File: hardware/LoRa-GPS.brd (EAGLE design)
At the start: 50.8 x 17.8 mm, 30 parts, among them J1 10118193-0001LF, Q1 IRLML6402, U1 MCP1703-3302E/CB, Y1 CRYSTAL.ABS07

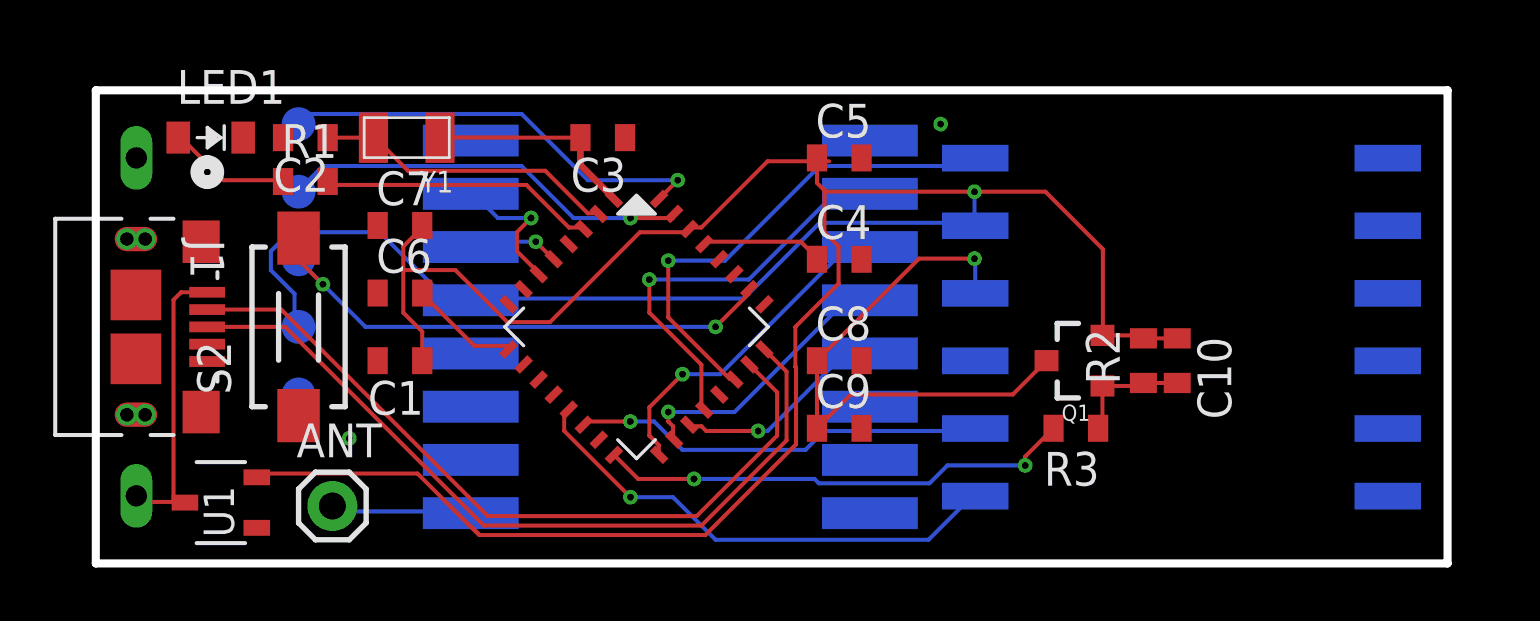
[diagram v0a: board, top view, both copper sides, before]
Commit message: DRC correct. CAM output
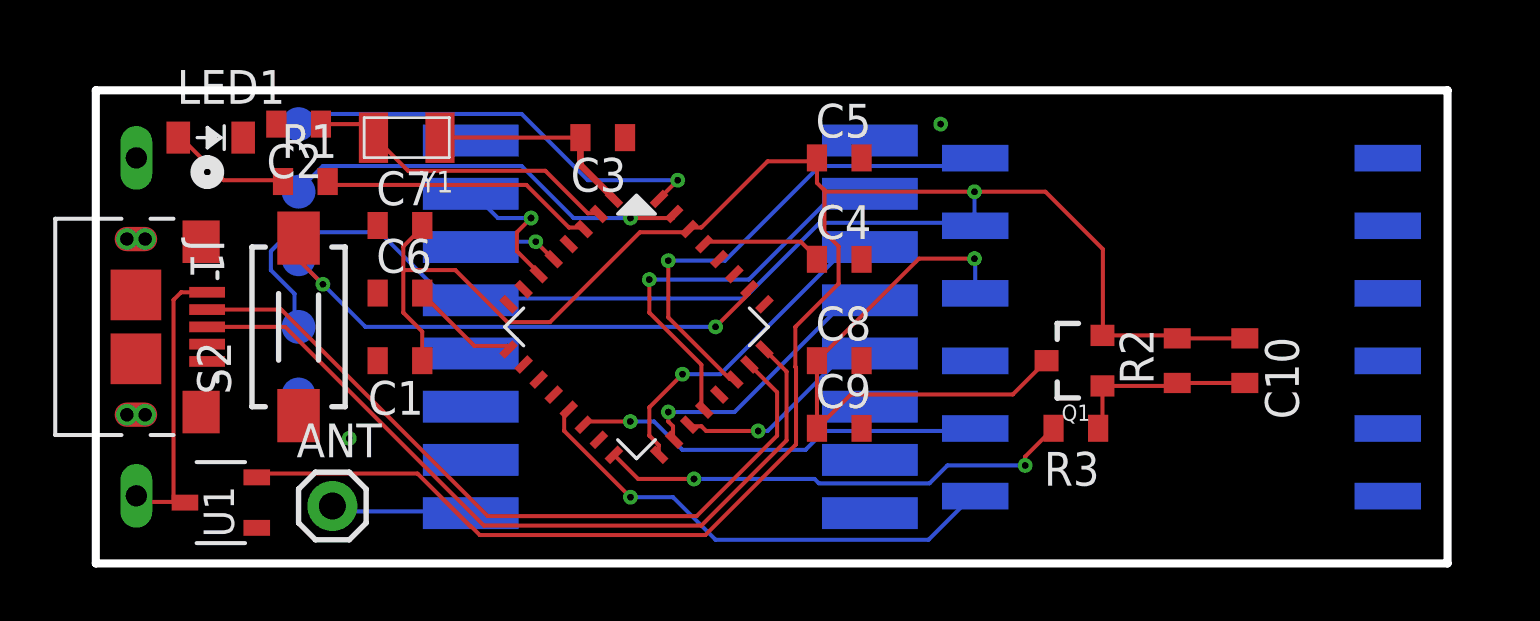
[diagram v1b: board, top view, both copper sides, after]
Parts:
- moved C10 2.54 mm to (43.2, 7.62)
- moved R2 1.27 mm to (40.6, 7.62)
- moved C2 0.57 mm to (7.62, 16.5)
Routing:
- net N$8: track 4.51 -> 7.05 mm
- net VCC: track 111.3 -> 112.8 mm
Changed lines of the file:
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@@
 <drawing>
 <settings>
-<setting alwaysvectorfont="yes"/>
+<setting alwaysvectorfont="no"/>
 <setting keepoldvectorfont="yes"/>
 <setting verticaltext="up"/>
@@
 <layer number="37" name="tTest" color="7" fill="1" visible="no" active="yes"/>
 <layer number="38" name="bTest" color="7" fill="1" visible="no" active="yes"/>
-<layer number="39" name="tKeepout" color="4" fill="11" visible="no" active="yes"/>
+<layer number="39" name="tKeepout" color="4" fill="11" visible="yes" active="yes"/>
 <layer number="40" name="bKeepout" color="1" fill="11" visible="no" active="yes"/>
 <layer number="41" name="tRestrict" color="4" fill="10" visible="no" active="yes"/>
@@
 <attribute name="VALUE" x="12.319" y="9.652" size="1.27" layer="27" rot="R180"/>
 </element>
-<element name="C2" library="nootropicdesign" package="C0603-THINCREAM" value="18pF" x="7.874" y="16.002" smashed="yes" rot="R180">
-<attribute name="MF" value="" x="7.874" y="16.002" size="1.778" layer="27" rot="R180" display="off"/>
-<attribute name="MPN" value="" x="7.874" y="16.002" size="1.778" layer="27" rot="R180" display="off"/>
-<attribute name="NAME" x="8.763" y="15.24" size="1.27" layer="25" rot="R180"/>
-<attribute name="OC_FARNELL" value="unknown" x="7.874" y="16.002" size="1.778" layer="27" rot="R180" display="off"/>
-<attribute name="VALUE" x="8.763" y="18.034" size="1.27" layer="27" rot="R180"/>
+<element name="C2" library="nootropicdesign" package="C0603-THINCREAM" value="18pF" x="7.62" y="16.51" smashed="yes" rot="R180">
+<attribute name="MF" value="" x="7.62" y="16.51" size="1.778" layer="27" rot="R180" display="off"/>
+<attribute name="MPN" value="" x="7.62" y="16.51" size="1.778" layer="27" rot="R180" display="off"/>
+<attribute name="NAME" x="8.509" y="15.748" size="1.27" layer="25" rot="R180"/>
+<attribute name="OC_FARNELL" value="unknown" x="7.62" y="16.51" size="1.778" layer="27" rot="R180" display="off"/>
+<attribute name="VALUE" x="8.509" y="18.542" size="1.27" layer="27" rot="R180"/>
 </element>
 <element name="C3" library="nootropicdesign" package="C0603-THINCREAM" value="18pF" x="19.05" y="16.002" smashed="yes" rot="R180">
@@
 <attribute name="VALUE" x="36.83" y="9.271" size="0.6096" layer="27" font="vector" ratio="20" rot="R180" align="top-center"/>
 </element>
-<element name="C10" library="nootropicdesign" package="C0603-THINCREAM" value="4.7uF" x="40.64" y="7.62" smashed="yes" rot="R270">
-<attribute name="MF" value="" x="40.64" y="7.62" size="1.778" layer="27" rot="R270" display="off"/>
-<attribute name="MPN" value="" x="40.64" y="7.62" size="1.778" layer="27" rot="R270" display="off"/>
-<attribute name="NAME" x="41.402" y="8.509" size="1.27" layer="25" rot="R270"/>
-<attribute name="OC_FARNELL" value="unknown" x="40.64" y="7.62" size="1.778" layer="27" rot="R270" display="off"/>
-<attribute name="VALUE" x="38.608" y="8.509" size="1.27" layer="27" rot="R270"/>
-</element>
-<element name="R2" library="nootropicdesign" package="R0603-THINCREAM" value="470" x="39.37" y="7.62" smashed="yes" rot="R90">
-<attribute name="MF" value="" x="39.37" y="7.62" size="1.778" layer="27" rot="R90" display="off"/>
-<attribute name="MPN" value="" x="39.37" y="7.62" size="1.778" layer="27" rot="R90" display="off"/>
-<attribute name="NAME" x="38.481" y="6.731" size="1.27" layer="25" rot="R90"/>
-<attribute name="OC_FARNELL" value="unknown" x="39.37" y="7.62" size="1.778" layer="27" rot="R90" display="off"/>
-<attribute name="VALUE" x="41.402" y="6.731" size="1.27" layer="27" rot="R90"/>
+<element name="C10" library="nootropicdesign" package="C0603-THINCREAM" value="4.7uF" x="43.18" y="7.62" smashed="yes" rot="R270">
+<attribute name="MF" value="" x="43.18" y="7.62" size="1.778" layer="27" rot="R270" display="off"/>
+<attribute name="MPN" value="" x="43.18" y="7.62" size="1.778" layer="27" rot="R270" display="off"/>
+<attribute name="NAME" x="43.942" y="8.509" size="1.27" layer="25" rot="R270"/>
+<attribute name="OC_FARNELL" value="unknown" x="43.18" y="7.62" size="1.778" layer="27" rot="R270" display="off"/>
+<attribute name="VALUE" x="41.148" y="8.509" size="1.27" layer="27" rot="R270"/>
+</element>
+<element name="R2" library="nootropicdesign" package="R0603-THINCREAM" value="470" x="40.64" y="7.62" smashed="yes" rot="R90">
+<attribute name="MF" value="" x="40.64" y="7.62" size="1.778" layer="27" rot="R90" display="off"/>
+<attribute name="MPN" value="" x="40.64" y="7.62" size="1.778" layer="27" rot="R90" display="off"/>
+<attribute name="NAME" x="39.751" y="6.731" size="1.27" layer="25" rot="R90"/>
+<attribute name="OC_FARNELL" value="unknown" x="40.64" y="7.62" size="1.778" layer="27" rot="R90" display="off"/>
+<attribute name="VALUE" x="42.672" y="6.731" size="1.27" layer="27" rot="R90"/>
 </element>
 <element name="R3" library="nootropicdesign" package="R0603-THINCREAM" value="2K2" x="36.83" y="5.08" smashed="yes" rot="R180">
@@
 <contactref element="TP2" pad="P$1"/>
 <via x="33.02" y="13.97" extent="1-16" drill="0.254"/>
-<wire x1="33.02" y1="13.97" x2="33.05" y2="13.94" width="0.254" layer="16"/>
 <wire x1="12.2682" y1="8.7122" x2="12.2682" y2="7.62" width="0.1524" layer="1"/>
 <wire x1="11.557" y1="9.4234" x2="12.2682" y2="8.7122" width="0.1524" layer="1"/>
@@
 <wire x1="14.0462" y1="9.9568" x2="14.09" y2="9.89" width="0.1524" layer="16"/>
 <wire x1="12.0904" y1="3.3782" x2="6.223" y2="3.3782" width="0.1524" layer="1"/>
-<wire x1="14.4018" y1="1.0668" x2="14.0843" y2="1.3843" width="0.1524" layer="1"/>
 <wire x1="14.0843" y1="1.3843" x2="12.0904" y2="3.3782" width="0.1524" layer="1"/>
 <wire x1="6.223" y1="3.3782" x2="6.049" y2="3.236" width="0.1524" layer="1"/>
@@
 <wire x1="32.893" y1="12.8016" x2="27.2034" y2="12.8016" width="0.1524" layer="16"/>
 <wire x1="14.224" y1="9.9568" x2="14.09" y2="9.89" width="0.1524" layer="16"/>
-<wire x1="27.559" y1="15.113" x2="27.2034" y2="15.113" width="0.1524" layer="1"/>
-<wire x1="27.2034" y1="15.113" x2="27.1018" y2="15.24" width="0.1524" layer="1"/>
 <contactref element="Q1" pad="2"/>
 <contactref element="C10" pad="1"/>
 <contactref element="R2" pad="2"/>
 <contactref element="GPS" pad="5"/>
-<wire x1="37.83" y1="8.57" x2="39.2582" y2="8.57" width="0.1524" layer="1"/>
-<wire x1="39.2582" y1="8.57" x2="39.37" y2="8.4582" width="0.1524" layer="1"/>
-<wire x1="39.37" y1="8.4582" x2="40.64" y2="8.4582" width="0.1524" layer="1"/>
+<wire x1="37.83" y1="8.57" x2="40.5282" y2="8.57" width="0.1524" layer="1"/>
+<wire x1="40.5282" y1="8.57" x2="40.64" y2="8.4582" width="0.1524" layer="1"/>
+<wire x1="40.64" y1="8.4582" x2="43.18" y2="8.4582" width="0.1524" layer="1"/>
 <wire x1="27.1018" y1="15.24" x2="27.1018" y2="14.3002" width="0.1524" layer="1"/>
 <wire x1="27.432" y1="13.97" x2="33.02" y2="13.97" width="0.1524" layer="1"/>
@@
 <wire x1="3.2004" y1="2.3114" x2="3.349" y2="2.286" width="0.1524" layer="1"/>
 <wire x1="1.6002" y1="2.4892" x2="1.524" y2="2.54" width="0.1524" layer="1"/>
-<wire x1="1.6002" y1="2.667" x2="1.524" y2="2.54" width="0.1524" layer="16"/>
 <contactref element="J1" pad="1"/>
 <wire x1="4.1827" y1="10.19" x2="3.205" y2="10.19" width="0.1524" layer="1"/>
@@
 <wire x1="18.8468" y1="13.1572" x2="18.905784375" y2="13.132640625" width="0.1524" layer="1"/>
 <wire x1="10.4902" y1="16.002" x2="10.434" y2="16.002" width="0.1524" layer="1"/>
-<wire x1="10.434" y1="16.002" x2="8.7122" y2="16.002" width="0.1524" layer="1"/>
+<wire x1="10.434" y1="16.002" x2="9.926" y2="16.51" width="0.1524" layer="1"/>
+<wire x1="9.926" y1="16.51" x2="8.4582" y2="16.51" width="0.1524" layer="1"/>
 </signal>
 <signal name="N$3">
@@
 <contactref element="C3" pad="2"/>
 <contactref element="SAMD21" pad="1"/>
-<wire x1="19.3802" y1="13.8684" x2="19.45505625" y2="13.728909375" width="0.1524" layer="1"/>
 <wire x1="19.45505625" y1="13.728909375" x2="19.47146875" y2="13.698325" width="0.1524" layer="1"/>
 <wire x1="12.934" y1="16.002" x2="18.2118" y2="16.002" width="0.1524" layer="1"/>
@@
 <contactref element="Q1" pad="1"/>
 <contactref element="R3" pad="1"/>
-<wire x1="40.64" y1="6.7818" x2="39.37" y2="6.7818" width="0.1524" layer="1"/>
-<wire x1="39.37" y1="6.7818" x2="39.2582" y2="6.67" width="0.1524" layer="1"/>
-<wire x1="39.2582" y1="6.67" x2="37.83" y2="6.67" width="0.1524" layer="1"/>
+<wire x1="43.18" y1="6.7818" x2="40.64" y2="6.7818" width="0.1524" layer="1"/>
+<wire x1="40.64" y1="6.7818" x2="40.5282" y2="6.67" width="0.1524" layer="1"/>
+<wire x1="40.5282" y1="6.67" x2="37.83" y2="6.67" width="0.1524" layer="1"/>
 <wire x1="37.83" y1="6.67" x2="37.83" y2="5.2418" width="0.1524" layer="1"/>
 <wire x1="37.83" y1="5.2418" x2="37.6682" y2="5.08" width="0.1524" layer="1"/>
@@
 <mfgpreviewcolor name="substratecolor" color="0xFF786E46"/>
 </mfgpreviewcolors>
+<errors>
+</errors>
 </board>
 </drawing>

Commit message: 470 to 47k
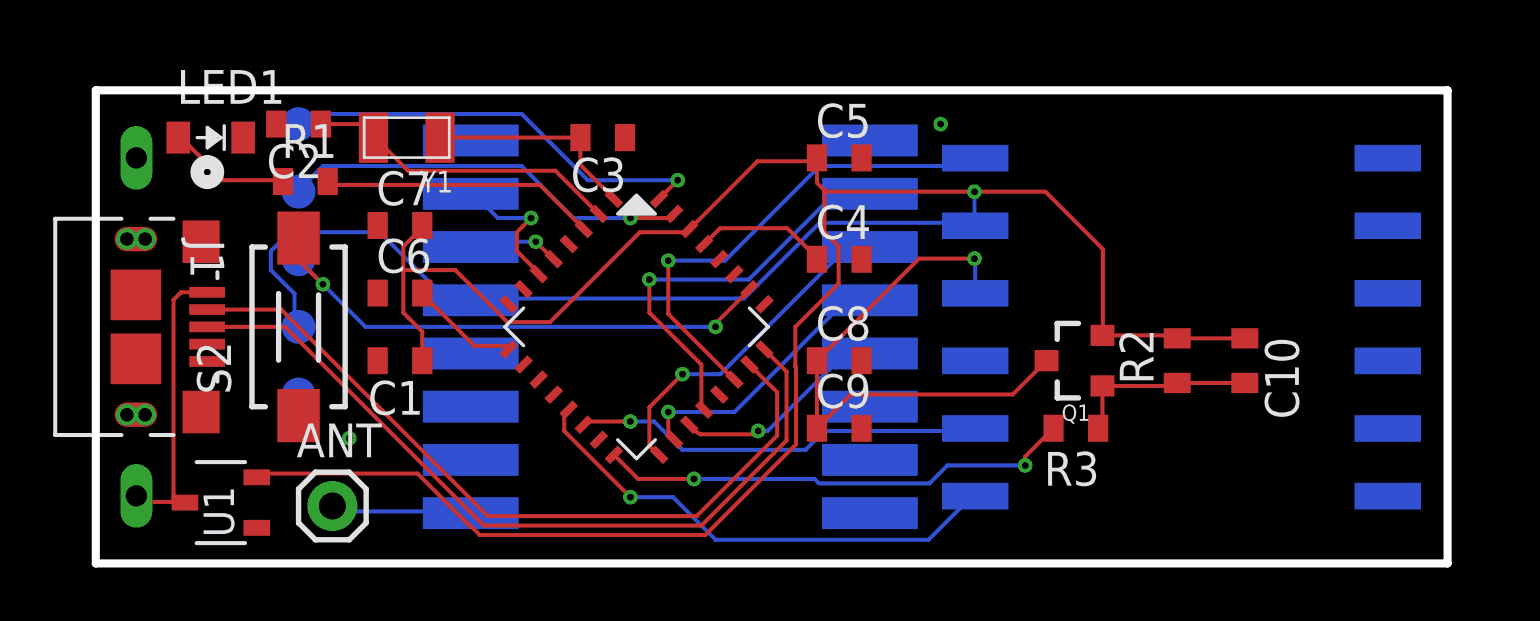
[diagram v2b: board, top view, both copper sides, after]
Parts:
- R2: value 470 -> 47k

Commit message: ripup
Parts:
- moved J1 47.6 mm to (49.1, 9.14), turned to 90 degrees
- moved JP2 47.4 mm to (48.9, 15.9)
- moved JP1 47.2 mm to (48.8, 2.41)
- moved U1 40.3 mm to (45.0, 2.41), turned to 270 degrees
- moved C2 9.03 mm to (16.6, 16.0)
- moved Y1 8.89 mm to (20.6, 16.0)
- moved LED1 8.64 mm to (13.0, 15.9)
- moved C3 5.08 mm to (24.1, 16.0)
- moved R1 4.71 mm to (12.6, 14.0)
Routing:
- net VCC: track 112.8 -> 0.00 mm, vias 1 -> 0
- net D+: track 30.0 -> 0.00 mm
- net D-: track 29.0 -> 0.00 mm
- net N$7: track 21.0 -> 0.00 mm, vias 1 -> 0
- net RESET: track 20.8 -> 0.00 mm, vias 2 -> 0
- net TX: track 18.7 -> 0.00 mm, vias 1 -> 0
- net D21: track 18.6 -> 0.00 mm, vias 1 -> 0
- net GPSPOWER: track 18.0 -> 0.00 mm, vias 2 -> 0
- net SWDIO: track 16.4 -> 0.00 mm, vias 1 -> 0
- net RX: track 15.5 -> 0.00 mm, vias 1 -> 0
- net SWCLK: track 15.5 -> 0.00 mm, vias 1 -> 0
- net MISO: track 15.4 -> 0.00 mm, vias 1 -> 0
- net MOSI: track 12.8 -> 0.00 mm, vias 1 -> 0
- net N$2: track 11.8 -> 0.00 mm
- net VIN: track 10.9 -> 0.00 mm
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
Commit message: Revert "ripup"
This reverts commit 834d71edbbdf070d64fbb4b16cb78b1eed2d9a3e.
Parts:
- moved J1 47.6 mm to (1.52, 8.89), turned to 270 degrees
- moved JP2 47.4 mm to (1.52, 15.2)
- moved JP1 47.2 mm to (1.52, 2.54)
- moved U1 40.3 mm to (4.70, 2.29), turned to 90 degrees
- moved C2 9.03 mm to (7.62, 16.5)
- moved Y1 8.89 mm to (11.7, 16.0)
- moved LED1 8.64 mm to (4.32, 16.0)
- moved C3 5.08 mm to (19.1, 16.0)
- moved R1 4.71 mm to (7.87, 14.4)
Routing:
- net VCC: track 0.00 -> 112.8 mm, vias 0 -> 1
- net D+: track 0.00 -> 30.0 mm
- net D-: track 0.00 -> 29.0 mm
- net N$7: track 0.00 -> 21.0 mm, vias 0 -> 1
- net RESET: track 0.00 -> 20.8 mm, vias 0 -> 2
- net TX: track 0.00 -> 18.7 mm, vias 0 -> 1
- net D21: track 0.00 -> 18.6 mm, vias 0 -> 1
- net GPSPOWER: track 0.00 -> 18.0 mm, vias 0 -> 2
- net SWDIO: track 0.00 -> 16.4 mm, vias 0 -> 1
- net RX: track 0.00 -> 15.5 mm, vias 0 -> 1
- net SWCLK: track 0.00 -> 15.5 mm, vias 0 -> 1
- net MISO: track 0.00 -> 15.4 mm, vias 0 -> 1
- net MOSI: track 0.00 -> 12.8 mm, vias 0 -> 1
- net N$2: track 0.00 -> 11.8 mm
- net VIN: track 0.00 -> 10.9 mm
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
